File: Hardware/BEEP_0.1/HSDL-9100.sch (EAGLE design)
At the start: 3 parts, among them IC1 HSDL-9100

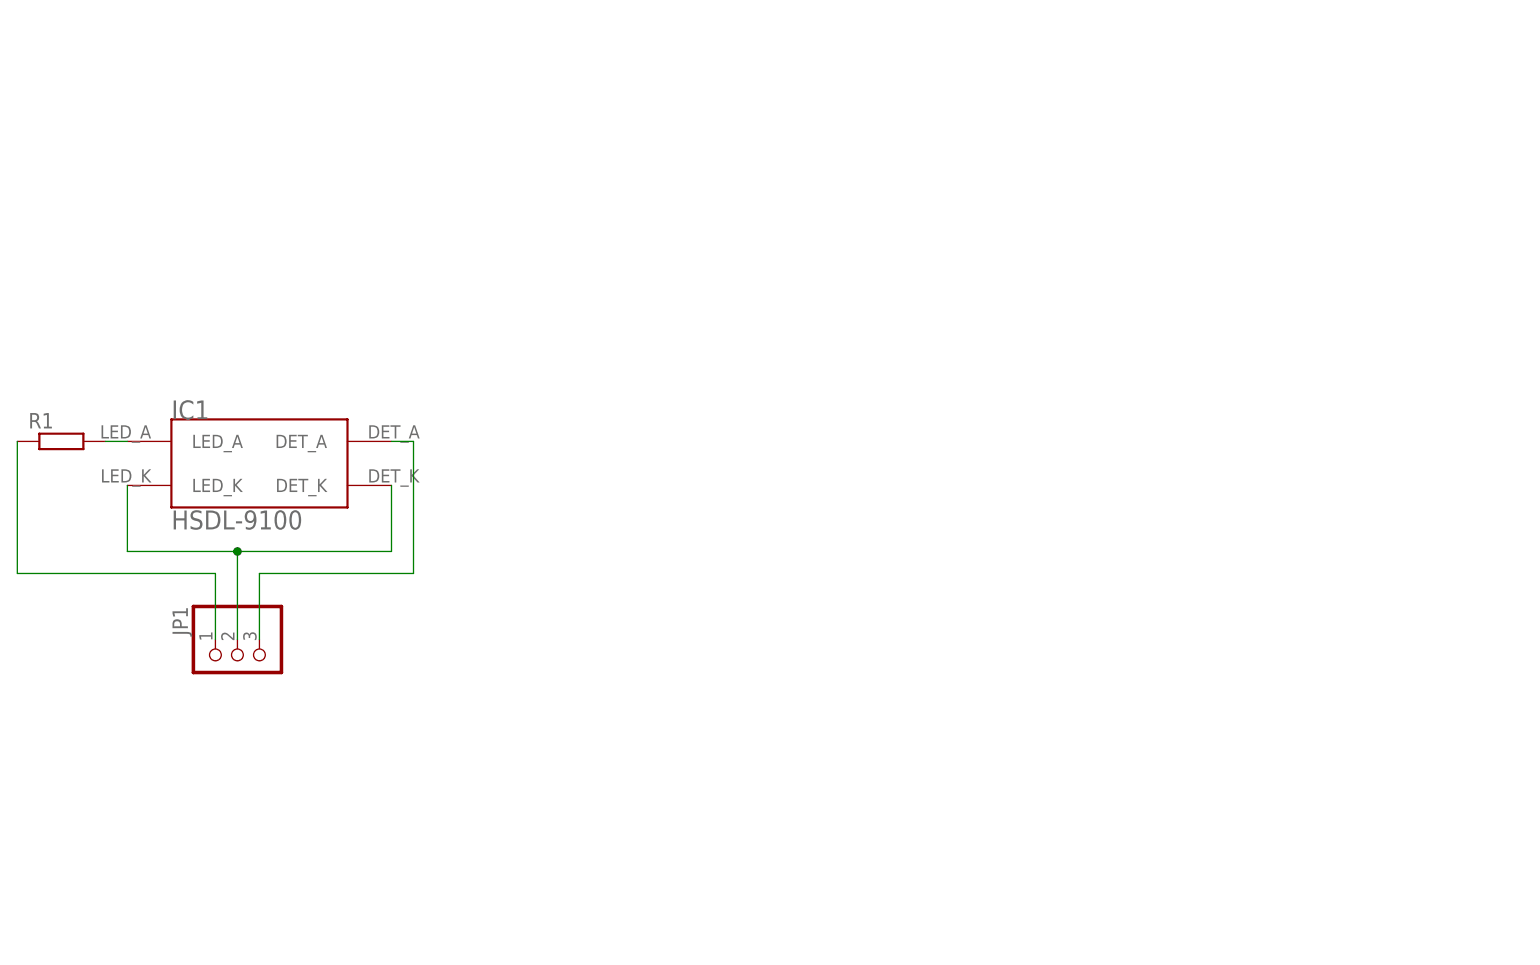
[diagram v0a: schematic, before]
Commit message: Add branding ;) enhance PCBs finish Easy RGB Board add Texas Instruments libray from Element 14 add dxf import ulp for eagle add Script for easy eagle export to pdf for etching minor cleanup
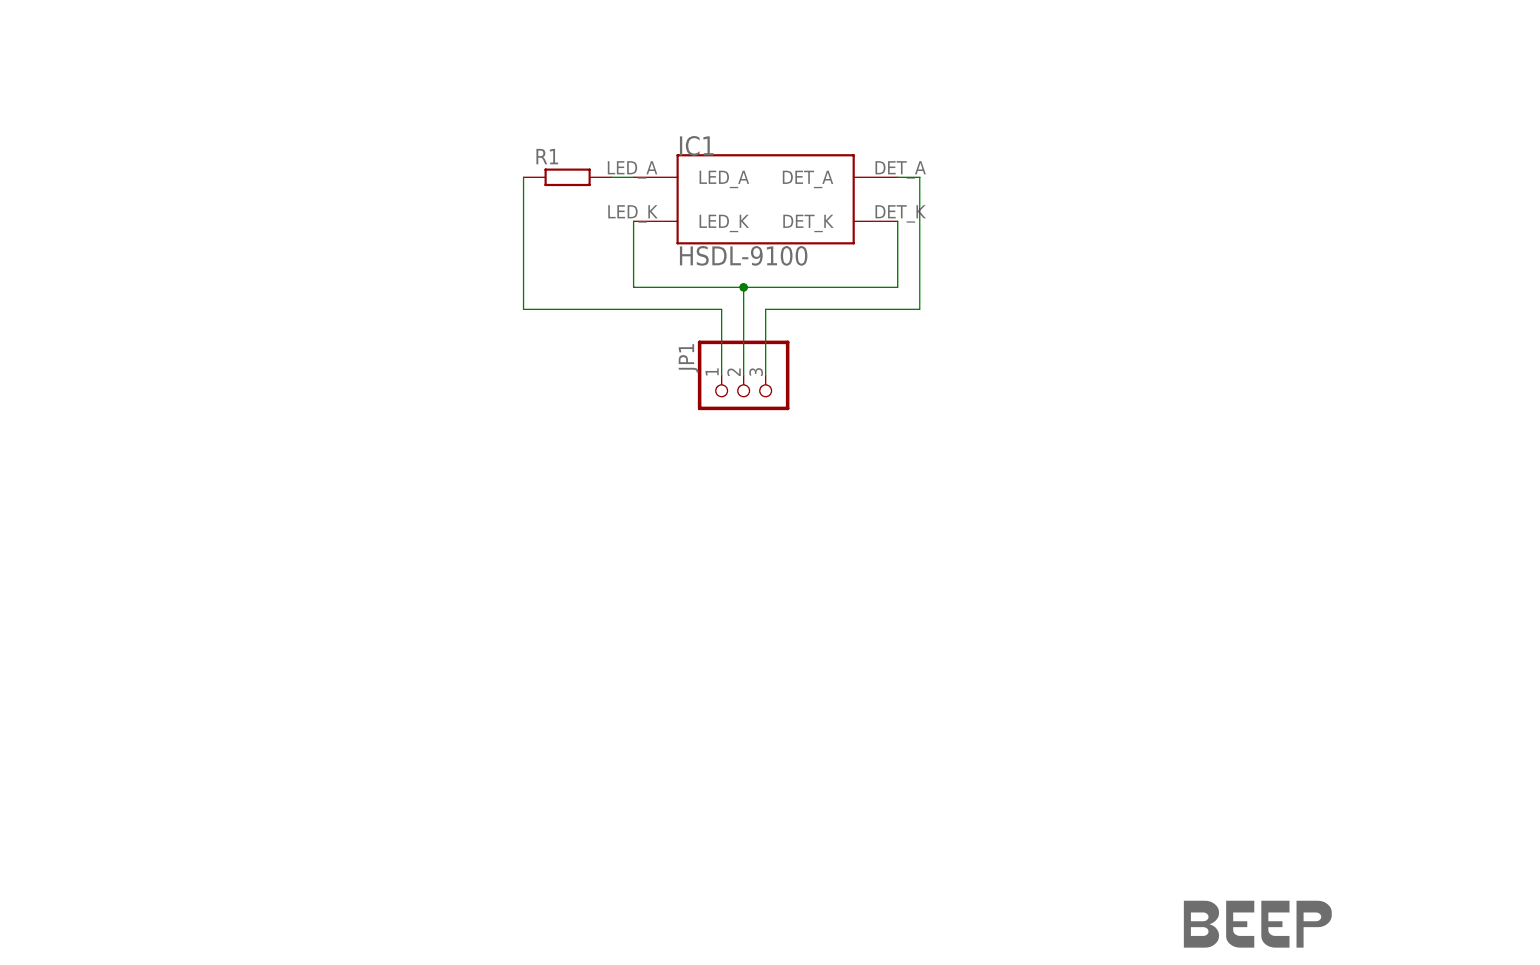
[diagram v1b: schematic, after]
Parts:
- added U$1: LOGO-COPPER3, Branding:LOGO-COPPER3
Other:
- moved on the sheet: IC1, JP1, R1
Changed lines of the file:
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@@
 <layer number="97" name="Info" color="7" fill="1" visible="yes" active="yes"/>
 <layer number="98" name="Guide" color="6" fill="1" visible="yes" active="yes"/>
+<layer number="100" name="tCName" color="7" fill="1" visible="yes" active="yes"/>
+<layer number="101" name="bCName" color="7" fill="1" visible="yes" active="yes"/>
 </layers>
 <schematic xreflabel="%F%N/%S.%C%R" xrefpart="/%S.%C%R">
@@
 <part name="R1" library="rcl" deviceset="R-EU_" device="M0805"/>
 <part name="JP1" library="pinhead" deviceset="PINHD-1X3" device=""/>
+<part name="FRAME1" library="frames" deviceset="A4L-LOC" device=""/>
+<part name="U$1" library="Branding" deviceset="LOGO-COPPER" device="3" value="LOGO-COPPER3"/>
 </parts>
 <sheets>
@@
 </plain>
 <instances>
-<instance part="IC1" gate="G$1" x="71.12" y="66.04"/>
-<instance part="R1" gate="G$1" x="48.26" y="68.58"/>
-<instance part="JP1" gate="A" x="68.58" y="43.18" rot="MR270"/>
+<instance part="IC1" gate="G$1" x="129.54" y="96.52"/>
+<instance part="R1" gate="G$1" x="106.68" y="99.06"/>
+<instance part="JP1" gate="A" x="127" y="73.66" rot="MR270"/>
+<instance part="FRAME1" gate="G$1" x="0" y="0"/>
+<instance part="U$1" gate="G$1" x="185.42" y="12.7"/>
 </instances>
 <busses>
@@
 <segment>
 <pinref part="IC1" gate="G$1" pin="LED_K"/>
-<wire x1="55.88" y1="63.5" x2="55.88" y2="55.88" width="0.1524" layer="91"/>
-<wire x1="55.88" y1="55.88" x2="68.58" y2="55.88" width="0.1524" layer="91"/>
+<wire x1="114.3" y1="93.98" x2="114.3" y2="86.36" width="0.1524" layer="91"/>
+<wire x1="114.3" y1="86.36" x2="127" y2="86.36" width="0.1524" layer="91"/>
 <pinref part="JP1" gate="A" pin="2"/>
-<wire x1="68.58" y1="55.88" x2="68.58" y2="45.72" width="0.1524" layer="91"/>
+<wire x1="127" y1="86.36" x2="127" y2="76.2" width="0.1524" layer="91"/>
 <pinref part="IC1" gate="G$1" pin="DET_K"/>
-<wire x1="86.36" y1="63.5" x2="86.36" y2="55.88" width="0.1524" layer="91"/>
-<wire x1="86.36" y1="55.88" x2="68.58" y2="55.88" width="0.1524" layer="91"/>
-<junction x="68.58" y="55.88"/>
+<wire x1="144.78" y1="93.98" x2="144.78" y2="86.36" width="0.1524" layer="91"/>
+<wire x1="144.78" y1="86.36" x2="127" y2="86.36" width="0.1524" layer="91"/>
+<junction x="127" y="86.36"/>
 </segment>
 </net>
@@
 <segment>
 <pinref part="R1" gate="G$1" pin="1"/>
-<wire x1="66.04" y1="53.34" x2="43.18" y2="53.34" width="0.1524" layer="91"/>
-<wire x1="43.18" y1="53.34" x2="43.18" y2="68.58" width="0.1524" layer="91"/>
+<wire x1="124.46" y1="83.82" x2="101.6" y2="83.82" width="0.1524" layer="91"/>
+<wire x1="101.6" y1="83.82" x2="101.6" y2="99.06" width="0.1524" layer="91"/>
 <pinref part="JP1" gate="A" pin="1"/>
-<wire x1="66.04" y1="53.34" x2="66.04" y2="45.72" width="0.1524" layer="91"/>
+<wire x1="124.46" y1="83.82" x2="124.46" y2="76.2" width="0.1524" layer="91"/>
 </segment>
 </net>
@@
 <pinref part="IC1" gate="G$1" pin="LED_A"/>
 <pinref part="R1" gate="G$1" pin="2"/>
-<wire x1="55.88" y1="68.58" x2="53.34" y2="68.58" width="0.1524" layer="91"/>
+<wire x1="114.3" y1="99.06" x2="111.76" y2="99.06" width="0.1524" layer="91"/>
 </segment>
 </net>
@@
 <segment>
 <pinref part="IC1" gate="G$1" pin="DET_A"/>
-<wire x1="86.36" y1="68.58" x2="88.9" y2="68.58" width="0.1524" layer="91"/>
-<wire x1="88.9" y1="53.34" x2="88.9" y2="68.58" width="0.1524" layer="91"/>
-<wire x1="88.9" y1="53.34" x2="71.12" y2="53.34" width="0.1524" layer="91"/>
+<wire x1="144.78" y1="99.06" x2="147.32" y2="99.06" width="0.1524" layer="91"/>
+<wire x1="147.32" y1="83.82" x2="147.32" y2="99.06" width="0.1524" layer="91"/>
+<wire x1="147.32" y1="83.82" x2="129.54" y2="83.82" width="0.1524" layer="91"/>
 <pinref part="JP1" gate="A" pin="3"/>
-<wire x1="71.12" y1="45.72" x2="71.12" y2="53.34" width="0.1524" layer="91"/>
+<wire x1="129.54" y1="76.2" x2="129.54" y2="83.82" width="0.1524" layer="91"/>
 </segment>
 </net>

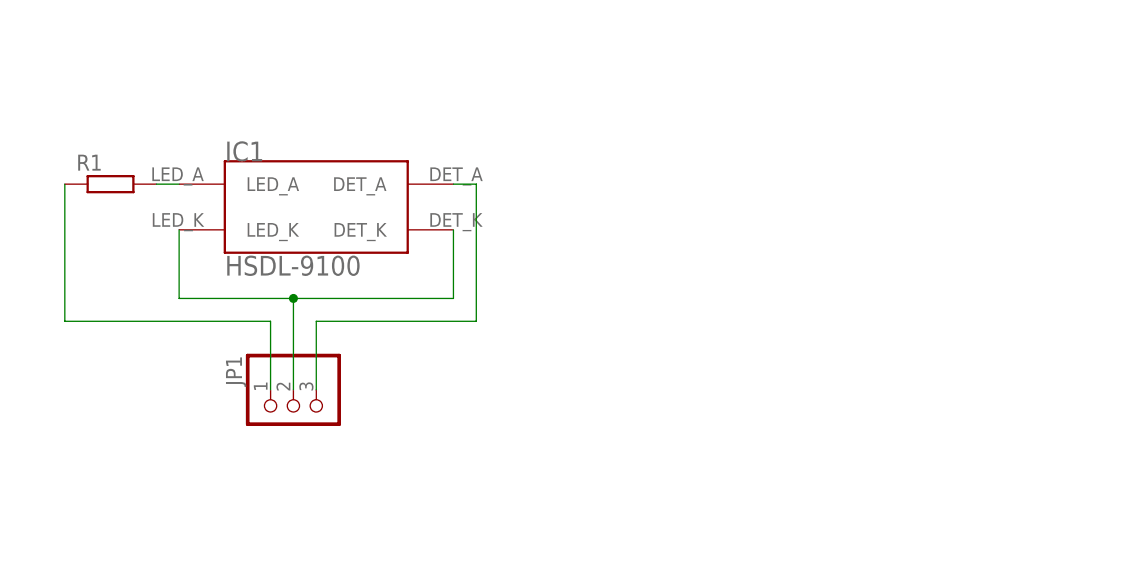
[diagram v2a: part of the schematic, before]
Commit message: enhance HSDL-9100 electronic
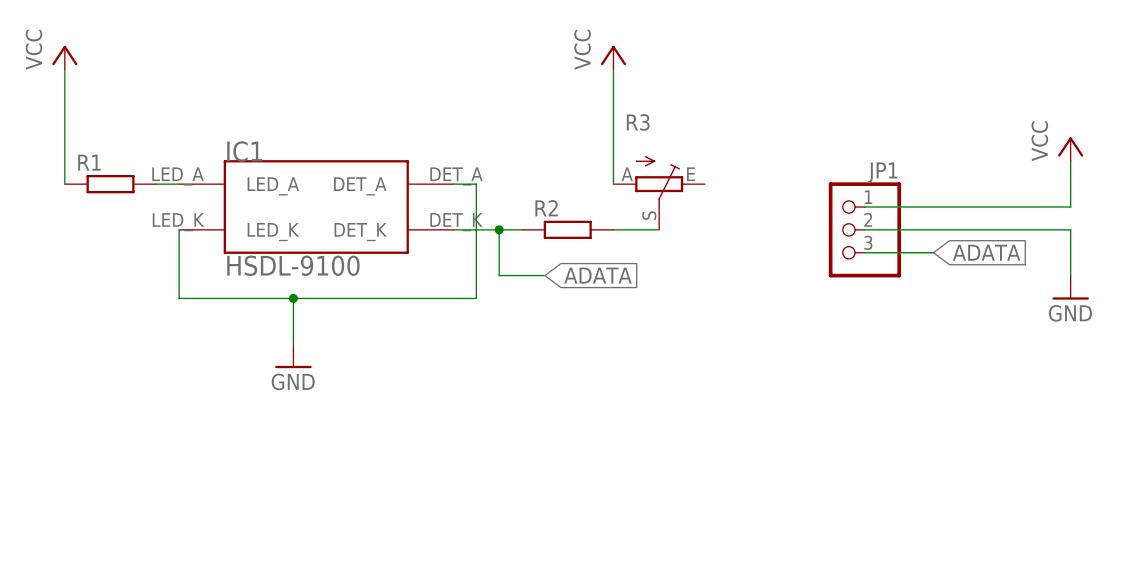
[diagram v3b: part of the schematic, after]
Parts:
- added R2: (no value), rcl:R-EU_M0805
- added R3: (no value), pot:TRIM_EU-B25P
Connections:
- removed net N$2: JP1.1, R1.1
- removed net N$4: IC1.DET_A, JP1.3
- new net ADATA: IC1.DET_K, JP1.3, R2.1
- new net N$5: R2.2, R3.S
- new net VCC: JP1.1, R1.1, R3.A
- net GND: now also IC1.DET_A; no longer IC1.DET_K
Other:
- moved on the sheet: JP1
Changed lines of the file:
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@@
 <part name="FRAME1" library="frames" deviceset="A4L-LOC" device=""/>
 <part name="U$1" library="Branding" deviceset="LOGO-COPPER" device="3" value="LOGO-COPPER3"/>
+<part name="R2" library="rcl" deviceset="R-EU_" device="M0805"/>
+<part name="R3" library="pot" deviceset="TRIM_EU-" device="B25P"/>
+<part name="P+1" library="supply1" deviceset="VCC" device=""/>
+<part name="P+2" library="supply1" deviceset="VCC" device=""/>
+<part name="GND1" library="supply1" deviceset="GND" device=""/>
+<part name="P+3" library="supply1" deviceset="VCC" device=""/>
+<part name="GND2" library="supply1" deviceset="GND" device=""/>
 </parts>
 <sheets>
@@
 <instance part="IC1" gate="G$1" x="129.54" y="96.52"/>
 <instance part="R1" gate="G$1" x="106.68" y="99.06"/>
-<instance part="JP1" gate="A" x="127" y="73.66" rot="MR270"/>
+<instance part="JP1" gate="A" x="187.96" y="93.98" rot="MR0"/>
 <instance part="FRAME1" gate="G$1" x="0" y="0"/>
 <instance part="U$1" gate="G$1" x="185.42" y="12.7"/>
+<instance part="R2" gate="G$1" x="157.48" y="93.98"/>
+<instance part="R3" gate="1" x="167.64" y="99.06" rot="R270"/>
+<instance part="P+1" gate="VCC" x="162.56" y="114.3"/>
+<instance part="P+2" gate="VCC" x="101.6" y="114.3"/>
+<instance part="GND1" gate="1" x="127" y="78.74"/>
+<instance part="P+3" gate="VCC" x="213.36" y="104.14"/>
+<instance part="GND2" gate="1" x="213.36" y="86.36"/>
 </instances>
 <busses>
@@
 <wire x1="114.3" y1="93.98" x2="114.3" y2="86.36" width="0.1524" layer="91"/>
 <wire x1="114.3" y1="86.36" x2="127" y2="86.36" width="0.1524" layer="91"/>
-<pinref part="JP1" gate="A" pin="2"/>
-<wire x1="127" y1="86.36" x2="127" y2="76.2" width="0.1524" layer="91"/>
-<pinref part="IC1" gate="G$1" pin="DET_K"/>
-<wire x1="144.78" y1="93.98" x2="144.78" y2="86.36" width="0.1524" layer="91"/>
-<wire x1="144.78" y1="86.36" x2="127" y2="86.36" width="0.1524" layer="91"/>
+<pinref part="GND1" gate="1" pin="GND"/>
+<pinref part="IC1" gate="G$1" pin="DET_A"/>
+<wire x1="127" y1="86.36" x2="127" y2="81.28" width="0.1524" layer="91"/>
+<wire x1="144.78" y1="99.06" x2="147.32" y2="99.06" width="0.1524" layer="91"/>
+<wire x1="147.32" y1="86.36" x2="147.32" y2="99.06" width="0.1524" layer="91"/>
+<wire x1="147.32" y1="86.36" x2="127" y2="86.36" width="0.1524" layer="91"/>
 <junction x="127" y="86.36"/>
 </segment>
-</net>
-<net name="N$2" class="0">
 <segment>
-<pinref part="R1" gate="G$1" pin="1"/>
-<wire x1="124.46" y1="83.82" x2="101.6" y2="83.82" width="0.1524" layer="91"/>
-<wire x1="101.6" y1="83.82" x2="101.6" y2="99.06" width="0.1524" layer="91"/>
-<pinref part="JP1" gate="A" pin="1"/>
-<wire x1="124.46" y1="83.82" x2="124.46" y2="76.2" width="0.1524" layer="91"/>
+<pinref part="GND2" gate="1" pin="GND"/>
+<wire x1="190.5" y1="93.98" x2="213.36" y2="93.98" width="0.1524" layer="91"/>
+<wire x1="213.36" y1="93.98" x2="213.36" y2="88.9" width="0.1524" layer="91"/>
+<pinref part="JP1" gate="A" pin="2"/>
 </segment>
 </net>
@@
 </segment>
 </net>
-<net name="N$4" class="0">
+<net name="ADATA" class="0">
 <segment>
-<pinref part="IC1" gate="G$1" pin="DET_A"/>
-<wire x1="144.78" y1="99.06" x2="147.32" y2="99.06" width="0.1524" layer="91"/>
-<wire x1="147.32" y1="83.82" x2="147.32" y2="99.06" width="0.1524" layer="91"/>
-<wire x1="147.32" y1="83.82" x2="129.54" y2="83.82" width="0.1524" layer="91"/>
+<pinref part="IC1" gate="G$1" pin="DET_K"/>
+<pinref part="R2" gate="G$1" pin="1"/>
+<wire x1="144.78" y1="93.98" x2="149.86" y2="93.98" width="0.1524" layer="91"/>
+<wire x1="149.86" y1="93.98" x2="152.4" y2="93.98" width="0.1524" layer="91"/>
+<wire x1="149.86" y1="93.98" x2="149.86" y2="88.9" width="0.1524" layer="91"/>
+<junction x="149.86" y="93.98"/>
+<wire x1="149.86" y1="88.9" x2="154.94" y2="88.9" width="0.1524" layer="91"/>
+<label x="154.94" y="88.9" size="1.778" layer="95" xref="yes"/>
+</segment>
+<segment>
 <pinref part="JP1" gate="A" pin="3"/>
-<wire x1="129.54" y1="76.2" x2="129.54" y2="83.82" width="0.1524" layer="91"/>
+<wire x1="190.5" y1="91.44" x2="198.12" y2="91.44" width="0.1524" layer="91"/>
+<label x="198.12" y="91.44" size="1.778" layer="95" xref="yes"/>
 </segment>
 </net>
+<net name="N$5" class="0">
+<segment>
+<pinref part="R2" gate="G$1" pin="2"/>
+<pinref part="R3" gate="1" pin="S"/>
+<wire x1="162.56" y1="93.98" x2="167.64" y2="93.98" width="0.1524" layer="91"/>
+</segment>
+</net>
+<net name="VCC" class="0">
+<segment>
+<pinref part="R3" gate="1" pin="A"/>
+<wire x1="162.56" y1="99.06" x2="162.56" y2="111.76" width="0.1524" layer="91"/>
+<pinref part="P+1" gate="VCC" pin="VCC"/>
+</segment>
+<segment>
+<pinref part="P+2" gate="VCC" pin="VCC"/>
+<pinref part="R1" gate="G$1" pin="1"/>
+<wire x1="101.6" y1="99.06" x2="101.6" y2="111.76" width="0.1524" layer="91"/>
+</segment>
+<segment>
+<pinref part="JP1" gate="A" pin="1"/>
+<pinref part="P+3" gate="VCC" pin="VCC"/>
+<wire x1="190.5" y1="96.52" x2="213.36" y2="96.52" width="0.1524" layer="91"/>
+<wire x1="213.36" y1="96.52" x2="213.36" y2="101.6" width="0.1524" layer="91"/>
+</segment>
+</net>
